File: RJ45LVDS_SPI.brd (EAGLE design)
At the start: 44.7 x 42.7 mm, 23 parts, among them J1 RJHSE-3381, U1 SN65MLVD206, U2 SN65MLVD206, U3 SN65MLVD206, U4 SN65MLVD206, U5 74ABT125PW, U7 MIC37100, X1 ELK-E333FA

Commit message: edits
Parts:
- moved U7 1.02 mm to (44.9, 53.9)
- moved C14 0.38 mm to (44.2, 48.3)
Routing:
- net MISO_IN: track 0.00 -> 30.5 mm
- net +5V: track 11.5 -> 41.8 mm
- net MOSI_OUT: track 0.00 -> 20.5 mm, vias 0 -> 1
- net SCLK_OUT: track 0.00 -> 11.4 mm, vias 0 -> 1
- net +3V3: track 78.7 -> 87.5 mm
- net SS_OUT: track 0.00 -> 2.54 mm
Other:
- board size 44.7 x 42.7 mm -> 44.8 x 37.8 mm
- board text added: "+4-6V"
- board text removed: "+5V"

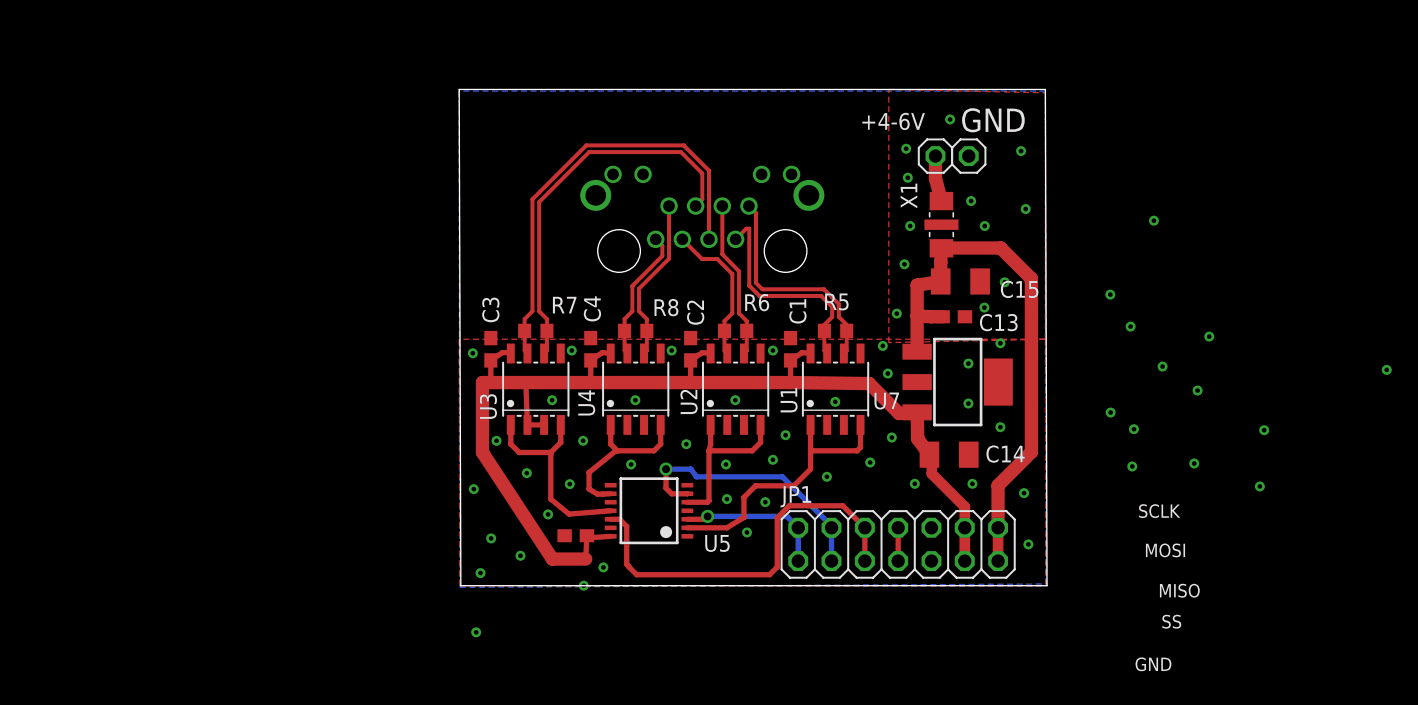
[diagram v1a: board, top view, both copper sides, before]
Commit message: added level translators
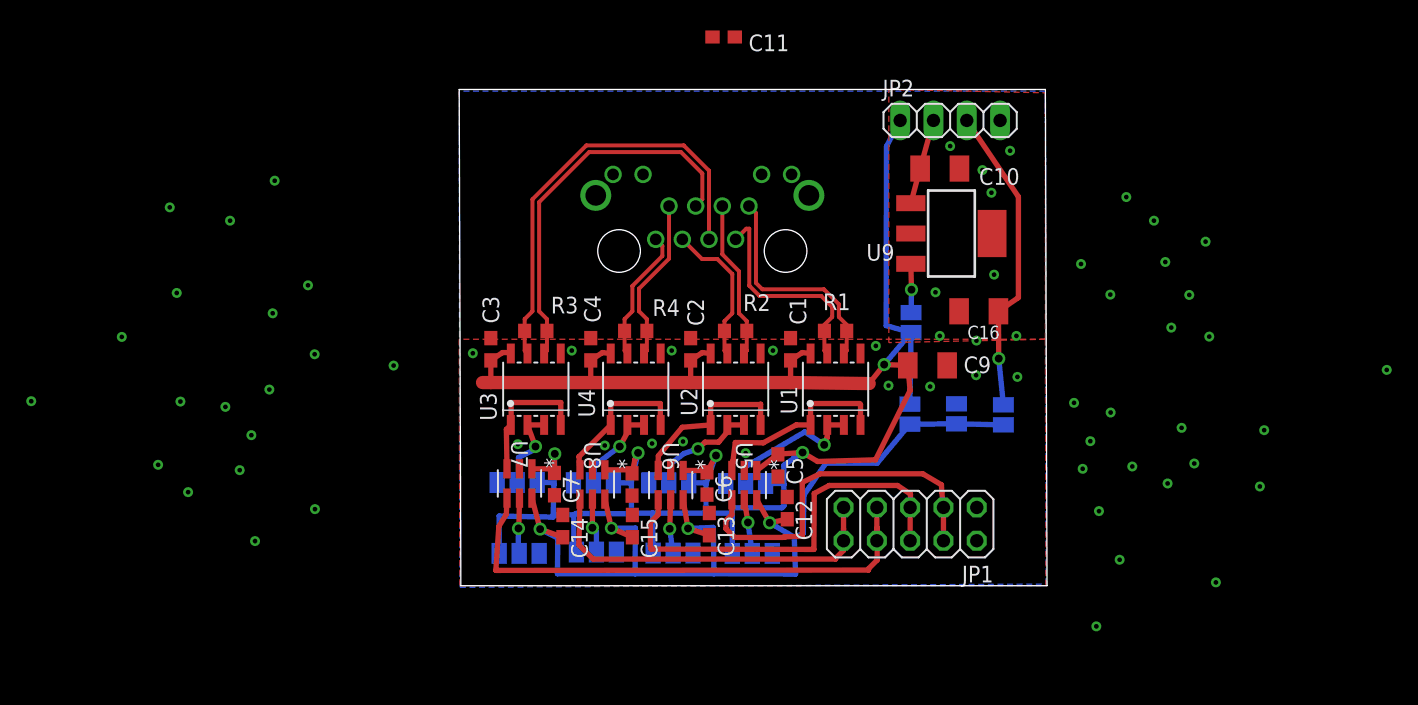
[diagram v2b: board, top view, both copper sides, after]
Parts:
- removed JP3, JP4: (no value), pinhead:1X01
- removed X1: ELK-E333FA, dds-boards:3218ELKE
- added C10, C16: 10u, rcl-dhs:C1206K
- added C11, C12, C5, C6, C7, C8: .1u, rcl-dhs:C0603
- added JP2: (no value), pinhead:1X04
- added SJ1, SJ2, SJ3, SJ4, SJ5, SJ6, SJ7, SJ8: (no value), jumper:SJ_2
- added SJ10, SJ11, SJ12, SJ9: (no value), jumper:SJ
- added U6, U8: SN74LVC1T45DBVR, SN74LVC1T45DBVR:DBV6
- added U9: MIC37100, dds-boards:SOT223
- C14, C15: value 10u -> .1u; device rcl-dhs:C1206K -> rcl-dhs:C0603
- C9: value .1u -> 10u; device rcl-dhs:C0603 -> rcl-dhs:C1206K
- JP1: device pinhead:2X07 -> pinhead:2X05
- U5: value 74ABT125PW -> SN74LVC1T45DBVR; device 74xx-us:TSSOP14 -> SN74LVC1T45DBVR:DBV6
- U7: value MIC37100 -> SN74LVC1T45DBVR; device dds-boards:SOT223 -> SN74LVC1T45DBVR:DBV6
- moved U7 34.3 mm to (11.5, 46.2)
- moved C15 31.2 mm to (20.1, 42.9), turned to 270 degrees
- moved C14 30.0 mm to (14.8, 42.9), turned to 270 degrees
- moved C9 29.8 mm to (42.6, 55.2), turned to 0 degrees
- moved C13 24.4 mm to (25.9, 43.1), turned to 270 degrees
- moved U5 7.52 mm to (28.6, 46.0), turned to 270 degrees
- moved JP1 1.80 mm to (41.2, 43.1), turned to 180 degrees
- renumbered R5 to R1, R6 to R2, R7 to R3, R8 to R4
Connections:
- removed net MISO: U3.1, U3.4, U5.11
- removed net MISO_IN: JP1.5, JP1.6, U5.12
- removed net MOSI: U2.1, U2.4, U5.5
- removed net MOSI_OUT: JP1.3, JP1.4, U5.6
- removed net N$20: JP3.1, X1.P$1
- removed net SCLK: U1.1, U1.4, U5.2
- removed net SCLK_OUT: JP1.1, JP1.2, U5.3
- removed net SS: U4.1, U4.4, U5.9
- removed net SS_OUT: JP1.7, JP1.8, U5.8
- new net 1_33: U1.1, U1.4, U5.3
- new net 2_33: U2.1, U2.4, U6.3
- new net 3_33: U3.1, U3.4, U7.3
- new net 4_33: U4.1, U4.4, U8.3
- new net N$10: SJ7.2, U7.5
- new net N$11: SJ6.2, U6.5
- new net N$12: C12.2, C13.2, C14.2, C15.2, SJ10.1, SJ11.1, SJ9.1, U5.6, U6.6, U7.6, U8.6
- new net N$13: JP1.3, JP1.4, U5.4
- new net N$14: JP1.5, JP1.6, U6.4
- new net N$15: JP1.7, JP1.8, U7.4
- new net N$16: C16.1, JP2.3, SJ11.2
- new net N$17: SJ12.1, U9.3
- new net N$3: SJ3.2, U3.2, U3.3
- new net N$4: SJ2.2, U2.2, U2.3
- new net N$5: SJ4.2, U4.2, U4.3
- new net N$6: SJ1.2, U1.2, U1.3
- new net N$7: SJ8.2, U8.5
- new net N$8: JP1.10, JP1.9, U8.4
- new net N$9: SJ5.2, U5.5
- net +3V3: now also C5.1, C6.1, C7.1, C8.1, JP2.1, SJ1.3, SJ12.2, SJ2.3, SJ3.3, SJ4.3, SJ5.1, SJ6.1, SJ7.1, SJ8.1, SJ9.2, U5.1, U6.1, U7.1, U8.1; no longer C14.1, JP1.11, JP1.12, U3.2, U3.3, U5.14, U7.3
- net +5V: now also C10.1, C11.1, JP2.2, SJ10.2, U9.1; no longer C13.1, C15.1, JP1.13, JP1.14, U7.1, X1.P$3
- net GND: now also C10.2, C11.2, C12.1, C13.1, C14.1, C15.1, C16.2, C5.2, C6.2, C7.2, C8.2, JP1.1, JP1.2, SJ1.1, SJ2.1, SJ3.1, SJ4.1, SJ5.3, SJ6.3, SJ7.3, SJ8.3, U5.2, U6.2, U8.2, U9.2, U9.4; no longer C13.2, C14.2, C15.2, JP1.10, JP1.9, JP4.1, U1.2, U1.3, U2.2, U2.3, U4.2, U4.3, U5.1, U5.10, U5.13, U5.4, U5.7, U7.4, X1.P$2
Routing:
- net N$12: track 0.00 -> 75.3 mm, vias 0 -> 4
- net +3V3: track 87.5 -> 160.5 mm, vias 0 -> 5
- net N$15: track 0.00 -> 41.1 mm
- net +5V: track 41.8 -> 6.54 mm
- net N$14: track 0.00 -> 32.0 mm
- net MISO_IN: track 30.5 -> 0.00 mm
- net N$8: track 0.00 -> 28.6 mm
- net N$13: track 0.00 -> 27.9 mm
- net N$16: track 0.00 -> 23.7 mm, vias 0 -> 1
- net SCLK: track 21.0 -> 0.00 mm
- net MOSI_OUT: track 20.5 -> 0.00 mm, vias 1 -> 0
- net MISO: track 15.8 -> 0.00 mm
- net 1_33: track 0.00 -> 15.3 mm
- net 2_33: track 0.00 -> 14.1 mm
- net MOSI: track 13.0 -> 0.00 mm
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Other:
- board text added: "1"
- board text added: "3"
- board text removed: "+4-6V"
- board text removed: "MISO"
- board text removed: "MOSI"
- board text removed: "SCLK"
- board text removed: "SS"

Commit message: documentation update
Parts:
- removed C11: .1u, rcl-dhs:C0603
- added R5: 100, rcl-dhs:R0603
- added SJ13: (no value), jumper:SJ
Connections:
- new net N$18: R5.2, SJ13.2
- new net N$19: J1.P$10, R5.1
- net +3V3: now also SJ13.1
- net +5V: no longer C11.1
- net GND: no longer C11.2, J1.P$10
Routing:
- net N$19: track 0.00 -> 4.63 mm
- net N$18: track 0.00 -> 4.46 mm, vias 0 -> 1
- net +3V3: track 160.5 -> 164.3 mm
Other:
- board size 44.8 x 37.8 mm -> 44.2 x 38 mm
- board text added: "2"
- board text added: "3.3"
- board text added: "4"
- board text added: "CH1"
- board text added: "CH2"
- board text added: "CH3"
- board text added: "CH4"
- board text added: "DIRECTION SET JUMPERS <- OUTPUT INPUT->"
- board text added: "EXT"
- board text added: "EXT V_LOGIC"
- board text added: "LED_EN"
- board text added: "REG_EN"
- board text added: "RJ45 LVDS breakout v1.0 NIST/DTCA/DHS 4/2017"
- board text added: "UNREG"
- board text added: "V_LOGIC"
- board text removed: "ARTIQ LVDS to SPI breakout v1.0 NIST/DTCA/DHS 4/2017"

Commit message: deleted backup files
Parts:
- R5: value 100 -> 750
- U9: value MIC37100 -> MIC39100-3.3WS
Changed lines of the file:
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@@
 <attribute name="VALUE" x="20.955" y="59.69" size="1.27" layer="27" rot="R180"/>
 </element>
-<element name="U9" library="dds-boards" package="SOT223" value="MIC37100" x="44.3992" y="65.2145" smashed="yes" rot="R270">
+<element name="U9" library="dds-boards" package="SOT223" value="MIC39100-3.3WS" x="44.3992" y="65.2145" smashed="yes" rot="R270">
 <attribute name="NAME" x="37.9095" y="63.1444" size="1.27" layer="25" font="vector" ratio="10"/>
 <attribute name="VALUE" x="43.0784" y="67.7545" size="1.27" layer="27" rot="R270"/>
@@
 <attribute name="VALUE" x="35.5917" y="74.295" size="0.02" layer="28" rot="MR0"/>
 </element>
-<element name="R5" library="rcl-dhs" package="R0603" value="100" x="29.9212" y="74.2696"/>
+<element name="R5" library="rcl-dhs" package="R0603" value="750" x="29.9212" y="74.2696"/>
 </elements>
 <signals>
